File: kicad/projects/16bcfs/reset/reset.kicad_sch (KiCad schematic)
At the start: 24 parts, among them J1 Conn_01x16_Pin, U10 74HC123, U11 74HC03, U2 74HC00, U3 74HC08, U4 74HC32, U5 74HC00, U7 74HC74, U8 74HC00, U9 74HC02

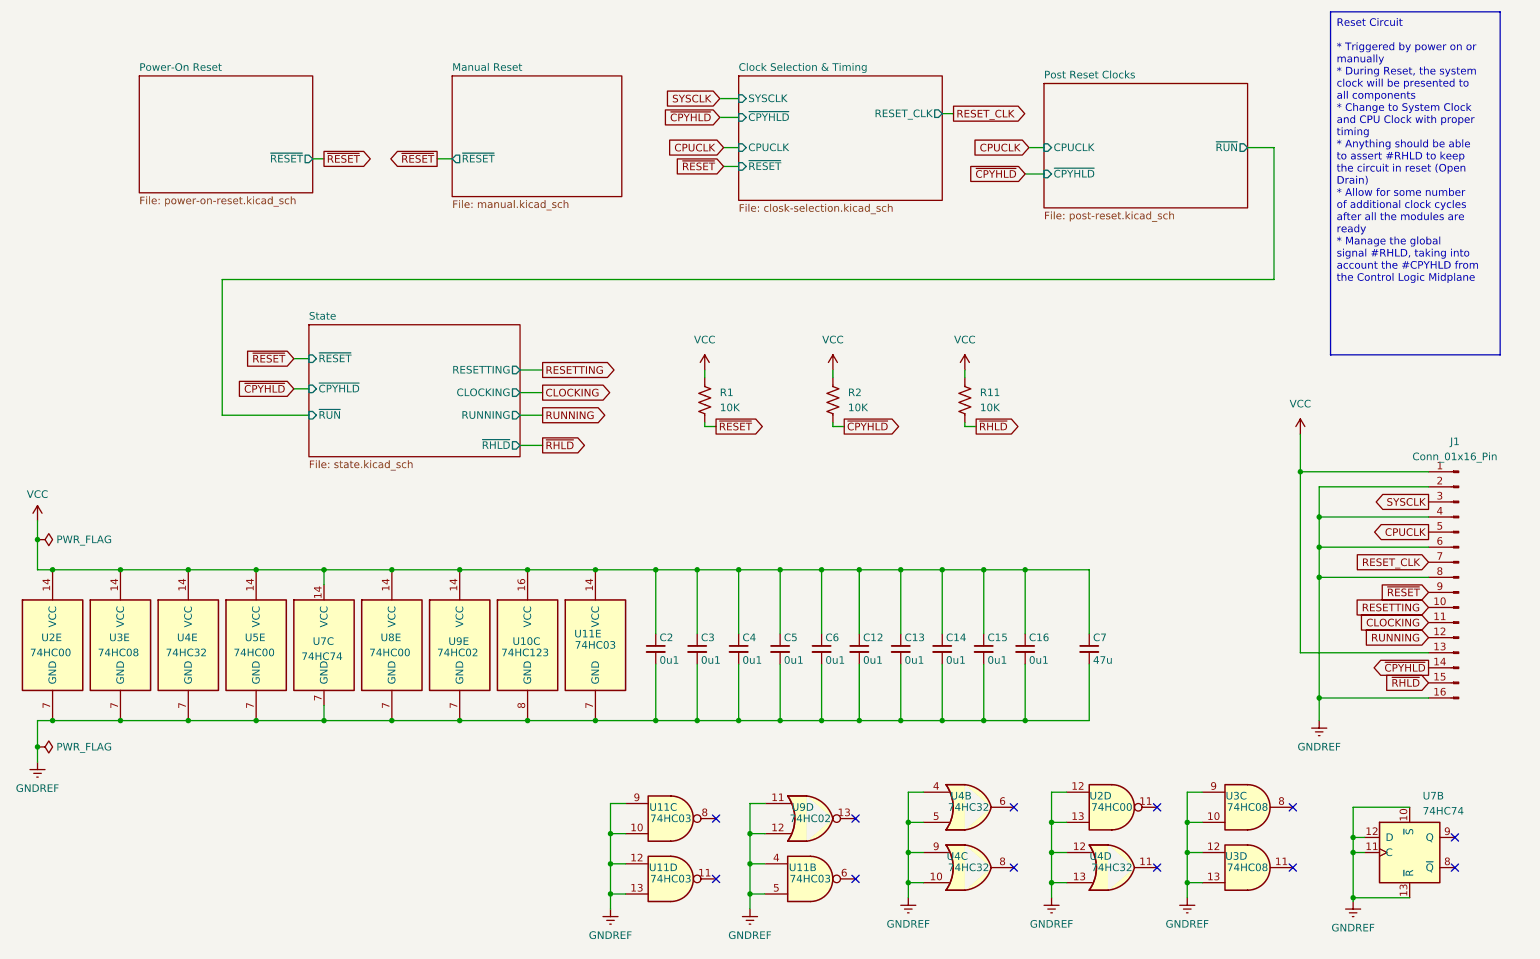
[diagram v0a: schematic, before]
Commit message: Added some debugging code
This is still not working.  I will need to revamp the reset routines for
the emulator to get this to work properly.  Everything will need an
initial state on construction and a `reset()` routine to place
everything into a proper state.  This in itself will be a major change.
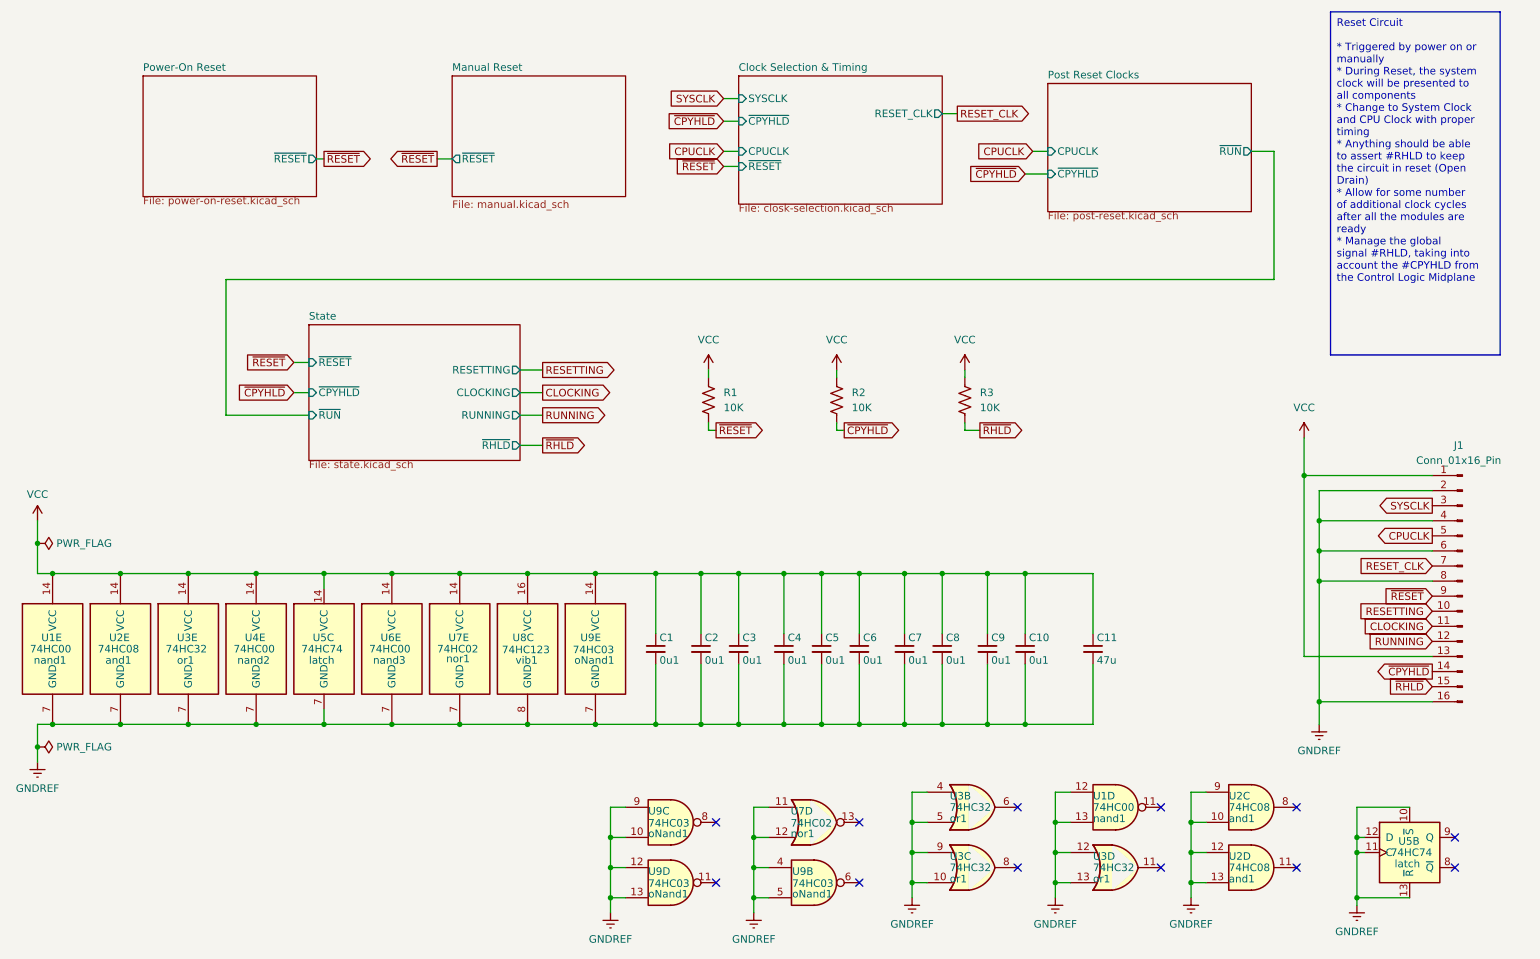
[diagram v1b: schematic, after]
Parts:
- U1: renamed from U2; name (none) -> nand1
- U2: renamed from U3; name (none) -> and1
- U3: renamed from U4; name (none) -> or1
- U4: renamed from U5; name (none) -> nand2
- U5: renamed from U7; name (none) -> latch
- U6: renamed from U8; name (none) -> nand3
- U7: renamed from U9; name (none) -> nor1
- U8: renamed from U10; name (none) -> vib1
- U9: renamed from U11; name (none) -> oNand1
- renumbered C2 to C1, C16 to C10, C7 to C11, C3 to C2, C4 to C3, C5 to C4, C6 to C5, C12 to C6, C13 to C7, C14 to C8, C15 to C9, R11 to R3
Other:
- moved on the sheet: C11, C2, C4, C7, C9, J1, R1, R2, U1D, U1E, U2C, U2D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

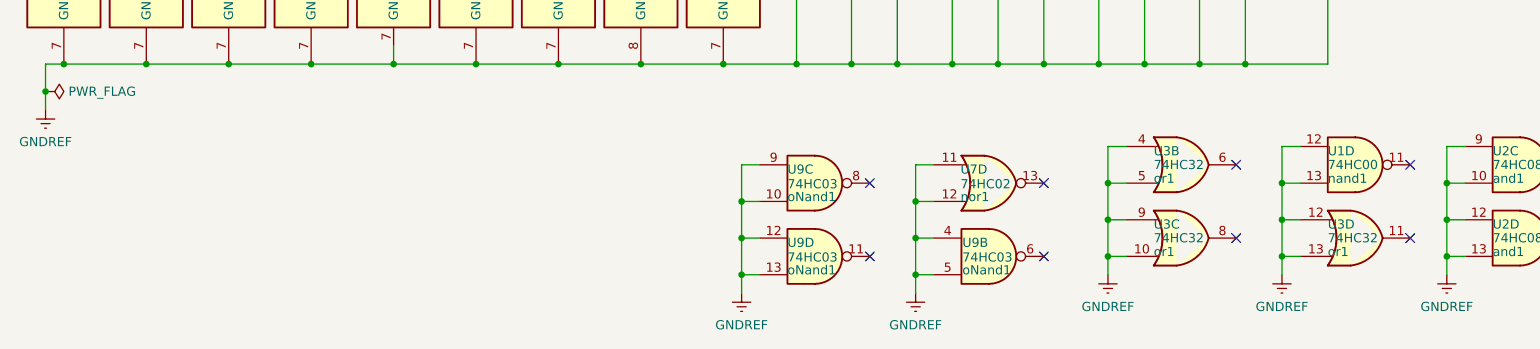
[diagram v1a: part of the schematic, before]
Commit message: Make a number of changes to the schematic and emulator
These changes are incremental to getting the emulator to work, they are
needed for making sure that the RESETTING, CLOCKING, and RUNNING signals
are processed properly.

There is also quite a bit of debugging code which gets added/removed
ahead of this commit.
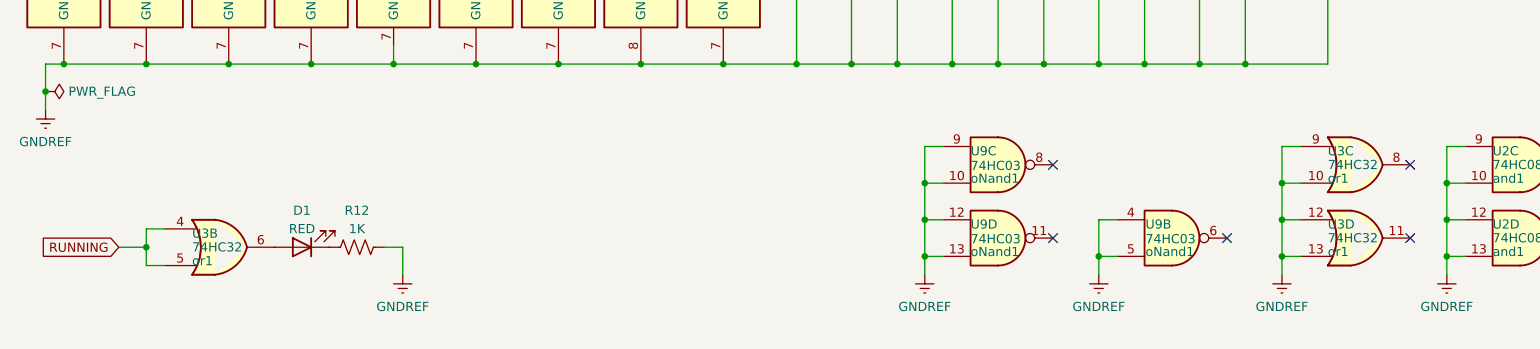
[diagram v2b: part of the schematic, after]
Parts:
- removed unit 4 of U1
- removed unit 4 of U7
- added D1: RED, symbol Device:LED
- added R12: 1K, symbol Device:R_US
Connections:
- net GNDREF: now also R12.2; no longer U3.4, U3.5
- net RUNNING: now also U3.4, U3.5
- net at U3.6: now also D1.2 (A)
- new net: D1.1 (K), R12.1
- no-connect marks 12 -> 9
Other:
- moved on the sheet: U3B, U3C, U9B, U9C, U9D

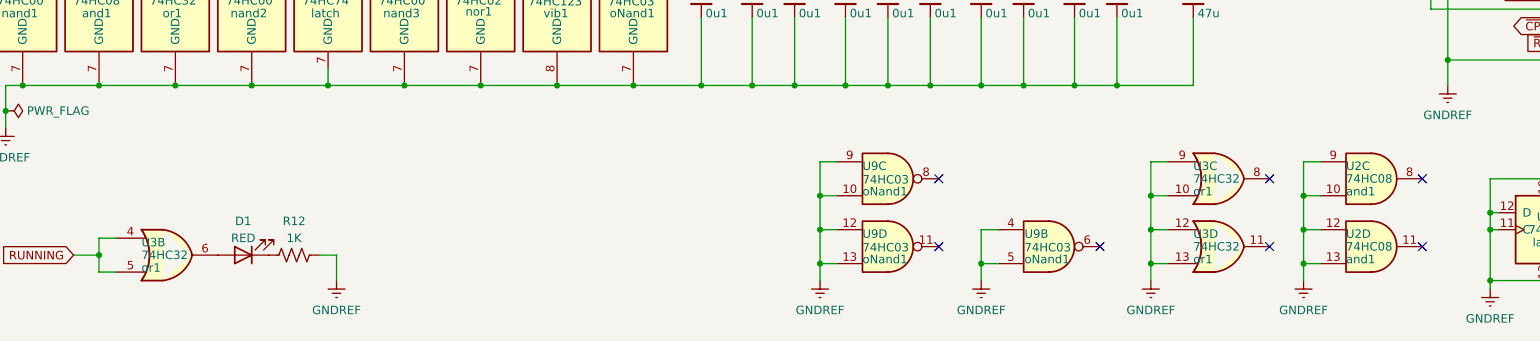
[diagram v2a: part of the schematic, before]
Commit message: Relocate the unused gates for efficiency
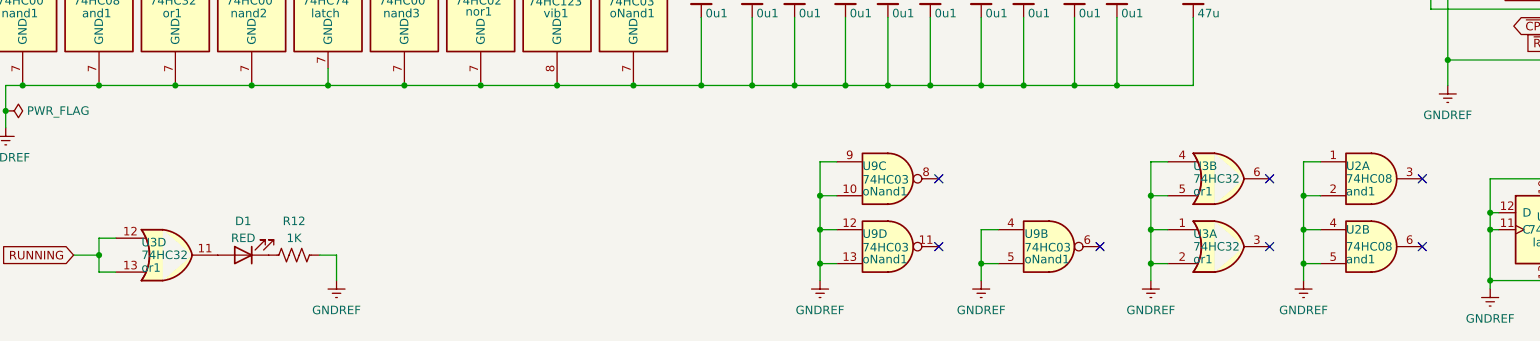
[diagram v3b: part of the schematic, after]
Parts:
- removed unit 4 of U2
- removed unit 3 of U2
- removed unit 3 of U3
- added unit 2 of U2
- added unit 1 of U2
- added unit 1 of U3
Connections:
- net GNDREF: now also U3.4, U3.5, U2.1, U2.2, U2.4, U2.5, U3.1, U3.2; no longer U3.12, U3.13
- net RUNNING: now also U3.12, U3.13; no longer U3.4, U3.5
- net at D1.2 (A): now also U3.11; no longer U3.6
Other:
- moved on the sheet: U3B, U3D
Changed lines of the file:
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@@
+    )
+  )
+  (symbol (lib_id "eryjus:74HC08") (at 222.25 160.02 0) (unit 2)
+    (in_bom yes) (on_board yes) (dnp no)
+    (property "Reference" "U2" (at 218.44 157.48 0)
+      (effects (font (size 1.27 1.27)) (justify left))
+    )
+    (property "Value" "74HC08" (at 218.44 160.02 0)
+      (effects (font (size 1.27 1.27)) (justify left))
+    )
+    (property "Footprint" "" (at 222.25 160.02 0)
+      (effects (font (size 1.27 1.27)) hide)
+    )
+    (property "Datasheet" "http://www.ti.com/lit/gpn/sn74HC08" (at 222.25 160.02 0)
+      (effects (font (size 1.27 1.27)) hide)
+    )
+    (property "name" "and1" (at 218.44 161.925 0)
+      (effects (font (size 1.27 1.27)) (justify left))
+    )
+    (pin "13")
+    (pin "10")
+    (pin "1")
+    (pin "12")
+    (pin "6")
+    (pin "3")
+    (pin "7")
+    (pin "14")
+    (pin "4")
+    (pin "11")
+    (pin "2")
+    (pin "5")
+    (pin "9")
+    (pin "8")
+    (instances
+      (project "reset"
+        (path "/d0ae44e5-d74e-4df6-bf3d-e0535c5a7785"
+          (reference "U2") (unit 2)
+        )
+      )
     )
   )
@@
     )
   )
+  (symbol (lib_id "eryjus:74HC08") (at 222.25 149.86 0) (unit 1)
+    (in_bom yes) (on_board yes) (dnp no)
+    (property "Reference" "U2" (at 218.44 147.955 0)
+      (effects (font (size 1.27 1.27)) (justify left))
+    )
+    (property "Value" "74HC08" (at 218.44 149.86 0)
+      (effects (font (size 1.27 1.27)) (justify left))
+    )
+    (property "Footprint" "" (at 222.25 149.86 0)
+      (effects (font (size 1.27 1.27)) hide)
+    )
+    (property "Datasheet" "http://www.ti.com/lit/gpn/sn74HC08" (at 222.25 149.86 0)
+      (effects (font (size 1.27 1.27)) hide)
+    )
+    (property "name" "and1" (at 218.44 151.765 0)
+      (effects (font (size 1.27 1.27)) (justify left))
+    )
+    (pin "13")
+    (pin "10")
+    (pin "1")
+    (pin "12")
+    (pin "6")
+    (pin "3")
+    (pin "7")
+    (pin "14")
+    (pin "4")
+    (pin "11")
+    (pin "2")
+    (pin "5")
+    (pin "9")
+    (pin "8")
+    (instances
+      (project "reset"
+        (path "/d0ae44e5-d74e-4df6-bf3d-e0535c5a7785"
+          (reference "U2") (unit 1)
+        )
+      )
+    )
+  )
   (symbol (lib_id "power:VCC") (at 173.99 76.2 0) (mirror y) (unit 1)
     (in_bom yes) (on_board yes) (dnp no)
@@
     )
   )
-  (symbol (lib_id "eryjus:74HC08") (at 222.25 160.02 0) (unit 4)
-    (in_bom yes) (on_board yes) (dnp no)
-    (property "Reference" "U2" (at 218.44 158.115 0)
-      (effects (font (size 1.27 1.27)) (justify left))
-    )
-    (property "Value" "74HC08" (at 218.44 160.02 0)
-      (effects (font (size 1.27 1.27)) (justify left))
-    )
-    (property "Footprint" "" (at 222.25 160.02 0)
-      (effects (font (size 1.27 1.27)) hide)
-    )
-    (property "Datasheet" "http://www.ti.com/lit/gpn/sn74HC08" (at 222.25 160.02 0)
-      (effects (font (size 1.27 1.27)) hide)
-    )
-    (property "name" "and1" (at 218.44 161.925 0)
-      (effects (font (size 1.27 1.27)) (justify left))
-    )
-    (pin "13")
-    (pin "10")
-    (pin "1")
-    (pin "12")
-    (pin "6")
-    (pin "3")
-    (pin "7")
-    (pin "14")
-    (pin "4")
-    (pin "11")
-    (pin "2")
-    (pin "5")
-    (pin "9")
-    (pin "8")
-    (instances
-      (project "reset"
-        (path "/d0ae44e5-d74e-4df6-bf3d-e0535c5a7785"
-          (reference "U2") (unit 4)
-        )
-      )
-    )
-  )
   (symbol (lib_id "74xx:74HC74") (at 66.04 123.19 0) (unit 3)
     (in_bom yes) (on_board yes) (dnp no)
@@
     )
   )
-  (symbol (lib_id "eryjus:74HC32") (at 199.39 149.86 0) (unit 3)
-    (in_bom yes) (on_board yes) (dnp no)
-    (property "Reference" "U3" (at 195.58 147.955 0)
-      (effects (font (size 1.27 1.27)) (justify left))
-    )
-    (property "Value" "74HC32" (at 195.58 149.86 0)
-      (effects (font (size 1.27 1.27)) (justify left))
-    )
-    (property "Footprint" "" (at 199.39 149.86 0)
-      (effects (font (size 1.27 1.27)) hide)
-    )
-    (property "Datasheet" "http://www.ti.com/lit/gpn/sn74HC32" (at 199.39 149.86 0)
-      (effects (font (size 1.27 1.27)) hide)
-    )
-    (property "name" "or1" (at 195.58 151.765 0)
-      (effects (font (size 1.27 1.27)) (justify left))
-    )
-    (pin "5")
-    (pin "4")
-    (pin "12")
-    (pin "1")
-    (pin "11")
-    (pin "6")
-    (pin "3")
-    (pin "14")
-    (pin "13")
-    (pin "7")
-    (pin "10")
-    (pin "2")
-    (pin "8")
-    (pin "9")
-    (instances
-      (project "reset"
-        (path "/d0ae44e5-d74e-4df6-bf3d-e0535c5a7785"
-          (reference "U3") (unit 3)
-        )
-      )
-    )
-  )
   (symbol (lib_id "Device:C_Small") (at 170.18 123.19 0) (unit 1)
     (in_bom yes) (on_board yes) (dnp no)
@@
     )
   )
-  (symbol (lib_id "eryjus:74HC08") (at 222.25 149.86 0) (unit 3)
-    (in_bom yes) (on_board yes) (dnp no)
-    (property "Reference" "U2" (at 218.44 147.955 0)
-      (effects (font (size 1.27 1.27)) (justify left))
-    )
-    (property "Value" "74HC08" (at 218.44 149.86 0)
-      (effects (font (size 1.27 1.27)) (justify left))
-    )
-    (property "Footprint" "" (at 222.25 149.86 0)
-      (effects (font (size 1.27 1.27)) hide)
-    )
-    (property "Datasheet" "http://www.ti.com/lit/gpn/sn74HC08" (at 222.25 149.86 0)
-      (effects (font (size 1.27 1.27)) hide)
-    )
-    (property "name" "and1" (at 218.44 151.765 0)
-      (effects (font (size 1.27 1.27)) (justify left))
-    )
-    (pin "13")
-    (pin "10")
-    (pin "1")
-    (pin "12")
-    (pin "6")
-    (pin "3")
-    (pin "7")
-    (pin "14")
-    (pin "4")
-    (pin "11")
-    (pin "2")
-    (pin "5")
-    (pin "9")
-    (pin "8")
-    (instances
-      (project "reset"
-        (path "/d0ae44e5-d74e-4df6-bf3d-e0535c5a7785"
-          (reference "U2") (unit 3)
-        )
-      )
-    )
-  )
   (symbol (lib_id "Device:R_US") (at 173.99 81.28 0) (unit 1)
     (in_bom yes) (on_board yes) (dnp no) (fields_autoplaced)
@@
     )
   )
-  (symbol (lib_id "eryjus:74HC32") (at 199.39 160.02 0) (unit 4)
-    (in_bom yes) (on_board yes) (dnp no)
-    (property "Reference" "U3" (at 195.58 158.115 0)
-      (effects (font (size 1.27 1.27)) (justify left))
-    )
-    (property "Value" "74HC32" (at 195.58 160.02 0)
-      (effects (font (size 1.27 1.27)) (justify left))
-    )
-    (property "Footprint" "" (at 199.39 160.02 0)
-      (effects (font (size 1.27 1.27)) hide)
-    )
-    (property "Datasheet" "http://www.ti.com/lit/gpn/sn74HC32" (at 199.39 160.02 0)
-      (effects (font (size 1.27 1.27)) hide)
-    )
-    (property "name" "or1" (at 195.58 161.925 0)
+  (symbol (lib_id "eryjus:74HC32") (at 41.91 161.29 0) (unit 4)
+    (in_bom yes) (on_board yes) (dnp no)
+    (property "Reference" "U3" (at 38.1 159.385 0)
+      (effects (font (size 1.27 1.27)) (justify left))
+    )
+    (property "Value" "74HC32" (at 38.1 161.29 0)
+      (effects (font (size 1.27 1.27)) (justify left))
+    )
+    (property "Footprint" "" (at 41.91 161.29 0)
+      (effects (font (size 1.27 1.27)) hide)
+    )
+    (property "Datasheet" "http://www.ti.com/lit/gpn/sn74HC32" (at 41.91 161.29 0)
+      (effects (font (size 1.27 1.27)) hide)
+    )
+    (property "name" "or1" (at 38.1 163.195 0)
       (effects (font (size 1.27 1.27)) (justify left))
     )
@@
     )
   )
-  (symbol (lib_id "eryjus:74HC32") (at 41.91 161.29 0) (unit 2)
-    (in_bom yes) (on_board yes) (dnp no)
-    (property "Reference" "U3" (at 38.1 159.385 0)
-      (effects (font (size 1.27 1.27)) (justify left))
-    )
-    (property "Value" "74HC32" (at 38.1 161.29 0)
-      (effects (font (size 1.27 1.27)) (justify left))
-    )
-    (property "Footprint" "" (at 41.91 161.29 0)
-      (effects (font (size 1.27 1.27)) hide)
-    )
-    (property "Datasheet" "http://www.ti.com/lit/gpn/sn74HC32" (at 41.91 161.29 0)
-      (effects (font (size 1.27 1.27)) hide)
-    )
-    (property "name" "or1" (at 38.1 163.195 0)
+  (symbol (lib_id "eryjus:74HC32") (at 199.39 149.86 0) (unit 2)
+    (in_bom yes) (on_board yes) (dnp no)
+    (property "Reference" "U3" (at 195.58 147.955 0)
+      (effects (font (size 1.27 1.27)) (justify left))
+    )
+    (property "Value" "74HC32" (at 195.58 149.86 0)
+      (effects (font (size 1.27 1.27)) (justify left))
+    )
+    (property "Footprint" "" (at 199.39 149.86 0)
+      (effects (font (size 1.27 1.27)) hide)
+    )
+    (property "Datasheet" "http://www.ti.com/lit/gpn/sn74HC32" (at 199.39 149.86 0)
+      (effects (font (size 1.27 1.27)) hide)
+    )
+    (property "name" "or1" (at 195.58 151.765 0)
       (effects (font (size 1.27 1.27)) (justify left))
     )
@@
         )
       )
+    )
+  )
+  (symbol (lib_id "eryjus:74HC32") (at 199.39 160.02 0) (unit 1)
+    (in_bom yes) (on_board yes) (dnp no)
+    (property "Reference" "U3" (at 195.58 158.115 0)
+      (effects (font (size 1.27 1.27)) (justify left))
+    )
+    (property "Value" "74HC32" (at 195.58 160.02 0)
+      (effects (font (size 1.27 1.27)) (justify left))
+    )
+    (property "Footprint" "" (at 199.39 160.02 0)
+      (effects (font (size 1.27 1.27)) hide)
+    )
+    (property "Datasheet" "http://www.ti.com/lit/gpn/sn74HC32" (at 199.39 160.02 0)
+      (effects (font (size 1.27 1.27)) hide)
+    )
+    (property "name" "or1" (at 195.58 161.925 0)
+      (effects (font (size 1.27 1.27)) (justify left))
+    )
+    (pin "5")
+    (pin "4")
+    (pin "12")
+    (pin "1")
+    (pin "11")
+    (pin "6")
+    (pin "3")
+    (pin "14")
+    (pin "13")
+    (pin "7")
+    (pin "10")
+    (pin "2")
+    (pin "8")
+    (pin "9")
+    (instances
+      (project "reset"
+        (path "/d0ae44e5-d74e-4df6-bf3d-e0535c5a7785"
+          (reference "U3") (unit 1)
+        )
+      )
